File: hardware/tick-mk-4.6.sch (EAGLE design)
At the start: 31 parts, among them IC1 ATMEGA328P, IC2 DS1307, IC3 L7805, Y1 16MHz, Y2 32.768kHz

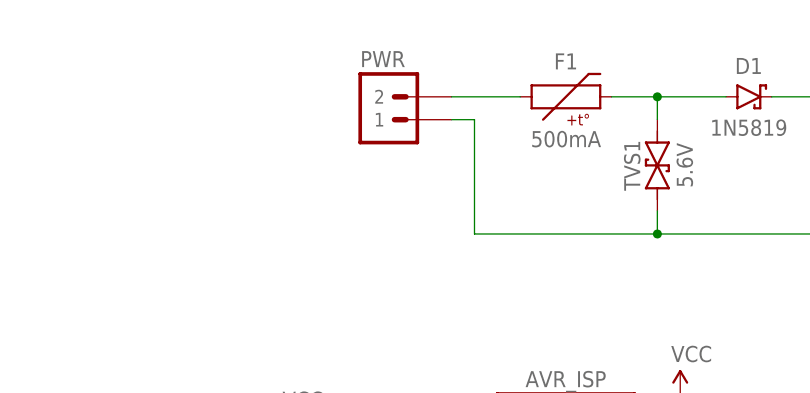
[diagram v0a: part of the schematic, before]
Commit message: reverting v4.4 and adding 4.6 for compromise between saner layout and all pth/on-hand parts design
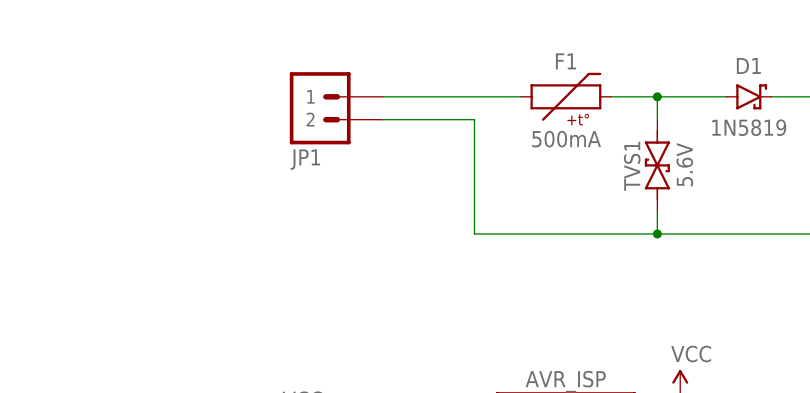
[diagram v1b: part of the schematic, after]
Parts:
- removed PWR: M02JST-PTH-VERT, A_butts:M02JST-PTH-VERT
- added JP1: M02JST-XH-VERT, A_butts:M02JST-XH-VERT
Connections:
- net GND: now also JP1.2; no longer PWR.1
- net N$7: now also JP1.1; no longer PWR.2
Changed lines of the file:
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@@
 <part name="IC3" library="A_butts" deviceset="V_REG_78XX" device="TO-220-THERMPAD" value="L7805"/>
 <part name="D1" library="A_butts" deviceset="DIODE-SCHOTTKY" device="PTH-10.16MM" value="1N5819"/>
-<part name="PWR" library="A_butts" deviceset="M02" device="JST-PTH-VERT"/>
 <part name="BAT1" library="A_butts" deviceset="BATTERY" device="20MMSMD-MINE" value="20mm coincell"/>
 <part name="GND1" library="A_butts" deviceset="GND" device=""/>
@@
 <part name="IC2" library="A_butts" deviceset="DS1307" device=""/>
 <part name="Y2" library="A_butts" deviceset="CRYSTAL" device="TC26H" value="32.768kHz"/>
+<part name="JP1" library="A_butts" deviceset="M02" device="JST-XH-VERT"/>
 </parts>
 <sheets>
@@
 <instance part="IC3" gate="G$1" x="147.32" y="208.28"/>
 <instance part="D1" gate="G$1" x="121.92" y="208.28"/>
-<instance part="PWR" gate="G$1" x="78.74" y="203.2"/>
 <instance part="BAT1" gate="G$1" x="264.16" y="144.78"/>
 <instance part="GND1" gate="1" x="271.78" y="139.7"/>
@@
 <instance part="IC2" gate="G$1" x="241.3" y="147.32"/>
 <instance part="Y2" gate="G$1" x="238.76" y="177.8" rot="MR0"/>
+<instance part="JP1" gate="G$1" x="71.12" y="210.82" rot="MR180"/>
 </instances>
 <busses>
@@
 <pinref part="C5" gate="G$1" pin="-"/>
 <pinref part="IC3" gate="G$1" pin="GND"/>
-<pinref part="PWR" gate="G$1" pin="1"/>
-<wire x1="88.9" y1="205.74" x2="91.44" y2="205.74" width="0.1524" layer="91"/>
 <wire x1="91.44" y1="205.74" x2="91.44" y2="193.04" width="0.1524" layer="91"/>
+<wire x1="81.28" y1="205.74" x2="91.44" y2="205.74" width="0.1524" layer="91"/>
+<pinref part="JP1" gate="G$1" pin="2"/>
 </segment>
 <segment>
@@
 </segment>
 </net>
-<net name="N$7" class="0">
-<segment>
-<pinref part="F1" gate="G$1" pin="1"/>
-<pinref part="PWR" gate="G$1" pin="2"/>
-<wire x1="88.9" y1="208.28" x2="96.52" y2="208.28" width="0.1524" layer="91"/>
-</segment>
-</net>
 <net name="N$8" class="0">
 <segment>
@@
 <pinref part="TVS1" gate="G$1" pin="2"/>
 <wire x1="111.76" y1="208.28" x2="111.76" y2="205.74" width="0.1524" layer="91"/>
-<pinref part="F1" gate="G$1" pin="2"/>
-<wire x1="106.68" y1="208.28" x2="111.76" y2="208.28" width="0.1524" layer="91"/>
 <pinref part="D1" gate="G$1" pin="A"/>
 <wire x1="111.76" y1="208.28" x2="119.38" y2="208.28" width="0.1524" layer="91"/>
+<wire x1="106.68" y1="208.28" x2="111.76" y2="208.28" width="0.1524" layer="91"/>
 <junction x="111.76" y="208.28"/>
+<pinref part="F1" gate="G$1" pin="2"/>
 </segment>
 </net>
@@
 </segment>
 </net>
+<net name="N$7" class="0">
+<segment>
+<pinref part="JP1" gate="G$1" pin="1"/>
+<wire x1="81.28" y1="208.28" x2="96.52" y2="208.28" width="0.1524" layer="91"/>
+<pinref part="F1" gate="G$1" pin="1"/>
+</segment>
+</net>
 </nets>
 </sheet>
 </sheets>
+<errors>
+</errors>
 </schematic>
 </drawing>
